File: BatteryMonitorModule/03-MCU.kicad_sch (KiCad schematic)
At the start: 0 parts

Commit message: schematic annotation and component placement for power supply, MCU, and power path sheets
Added symbol libraries (AP63203, AP63205, MIC5219, TC2117), annotated
ref designators, and placed components via MCP server. Includes
fix_sheet_instances.py utility for restoring sheet_instances blocks.

Co-Authored-By: Claude Opus 4.6 (1M context) <noreply@anthropic.com>
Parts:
- added C10, C6, C8, C9: 100nF, symbol Device:C
- added C7: 4.7uF, symbol Device:C
- added FB1: 600R@100MHz, symbol Device:L
- added J3: Conn_ARM_JTAG_SWD_10, symbol Connector:Conn_ARM_JTAG_SWD_10
- added J4: USB-C, symbol Connector:USB_C_Receptacle
- added R10: 10k, symbol Device:R
- added R11, R12, R13, R14: 4k7, symbol Device:R
- added R14, R15: 5k1, symbol Device:R
- added SW1: BOOT0, symbol Switch:SW_Push
- added SW2: NRST, symbol Switch:SW_Push
- added U1: STM32G0B1CCT6, symbol MCU_ST_STM32G0:STM32G0B1CCTx
- added U2: INA226AQDGSRQ1, symbol INA226AQDGSRQ1:INA226AQDGSRQ1
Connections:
- new net: FB1.1, U2.7 (GND)
- new net: J4.A5 (CC1), R14.1
- new net: J4.B5 (CC2), R15.1
- new net +3.3V: C10.1, C6.1, C7.1, C9.2, J3.1 (VTref), R11.1, R12.1, R13.1, R14.1, SW1.2, U1.4 (VBAT), U1.5 (VREF+), U1.6 (VDD), U2.6 (VS)
- new net +5VUsb: J4.A4 (VBUS), J4.A9 (VBUS), J4.B4 (VBUS), J4.B9 (VBUS)
- new net BOOT0/SWDCLK: J3.4 (SWCLK/TCK), R10.1, SW1.1, U1.36 (PA14)
- new net GND: C6.2, C7.2, C8.1, C9.1, FB1.2, J3.3 (GND), J3.5 (GND), J3.8 (NC/TDI), J3.9 (GNDDetect), J4.A1 (GND), J4.A10 (RX2-), J4.A11 (RX2+), J4.A12 (GND), J4.A2 (TX1+), J4.A3 (TX1-), J4.A8 (SBU1), J4.B1 (GND), J4.B10 (RX1-), J4.B11 (RX1+), J4.B12 (GND), J4.B2 (TX2+), J4.B3 (TX2-), J4.B8 (SBU2), J4.S1 (SHIELD), R10.2, R14.2, R15.2, SW2.1, U1.7 (VSS), U2.1 (A1), U2.2 (A0)
- new net I2C1_SCL: R11.2
- new net I2C1_SDA: R12.2
- new net I2C2_SCL: R13.2
- new net I2C2_SDA: R14.2
- new net INA_ALERT: U1.19 (PB0)
- new net N_RST: C8.2, J3.10 (~{RESET}), SW2.2, U1.10 (PF2)
- new net SHUNT_N: U2.9 (VIN-)
- new net SHUNT_P: U2.10 (VIN+), U2.8 (VBUS)
- new net SWDIO: J3.2 (SWDIO/TMS), U1.35 (PA13)
- new net SWO: J3.6 (SWO/TDO)
- new net USB_DN: J4.A7 (D-), J4.B7 (D-), U1.33 (PA9/PA11)
- new net USB_DP: J4.A6 (D+), J4.B6 (D+), U1.34 (PA10/PA12)
- new net VBUS_SENSE: U1.29 (PA9/UCPD1_DBCC1)
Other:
- note added: "I2C 0x40"
- note added: "I2C Pull Ups"

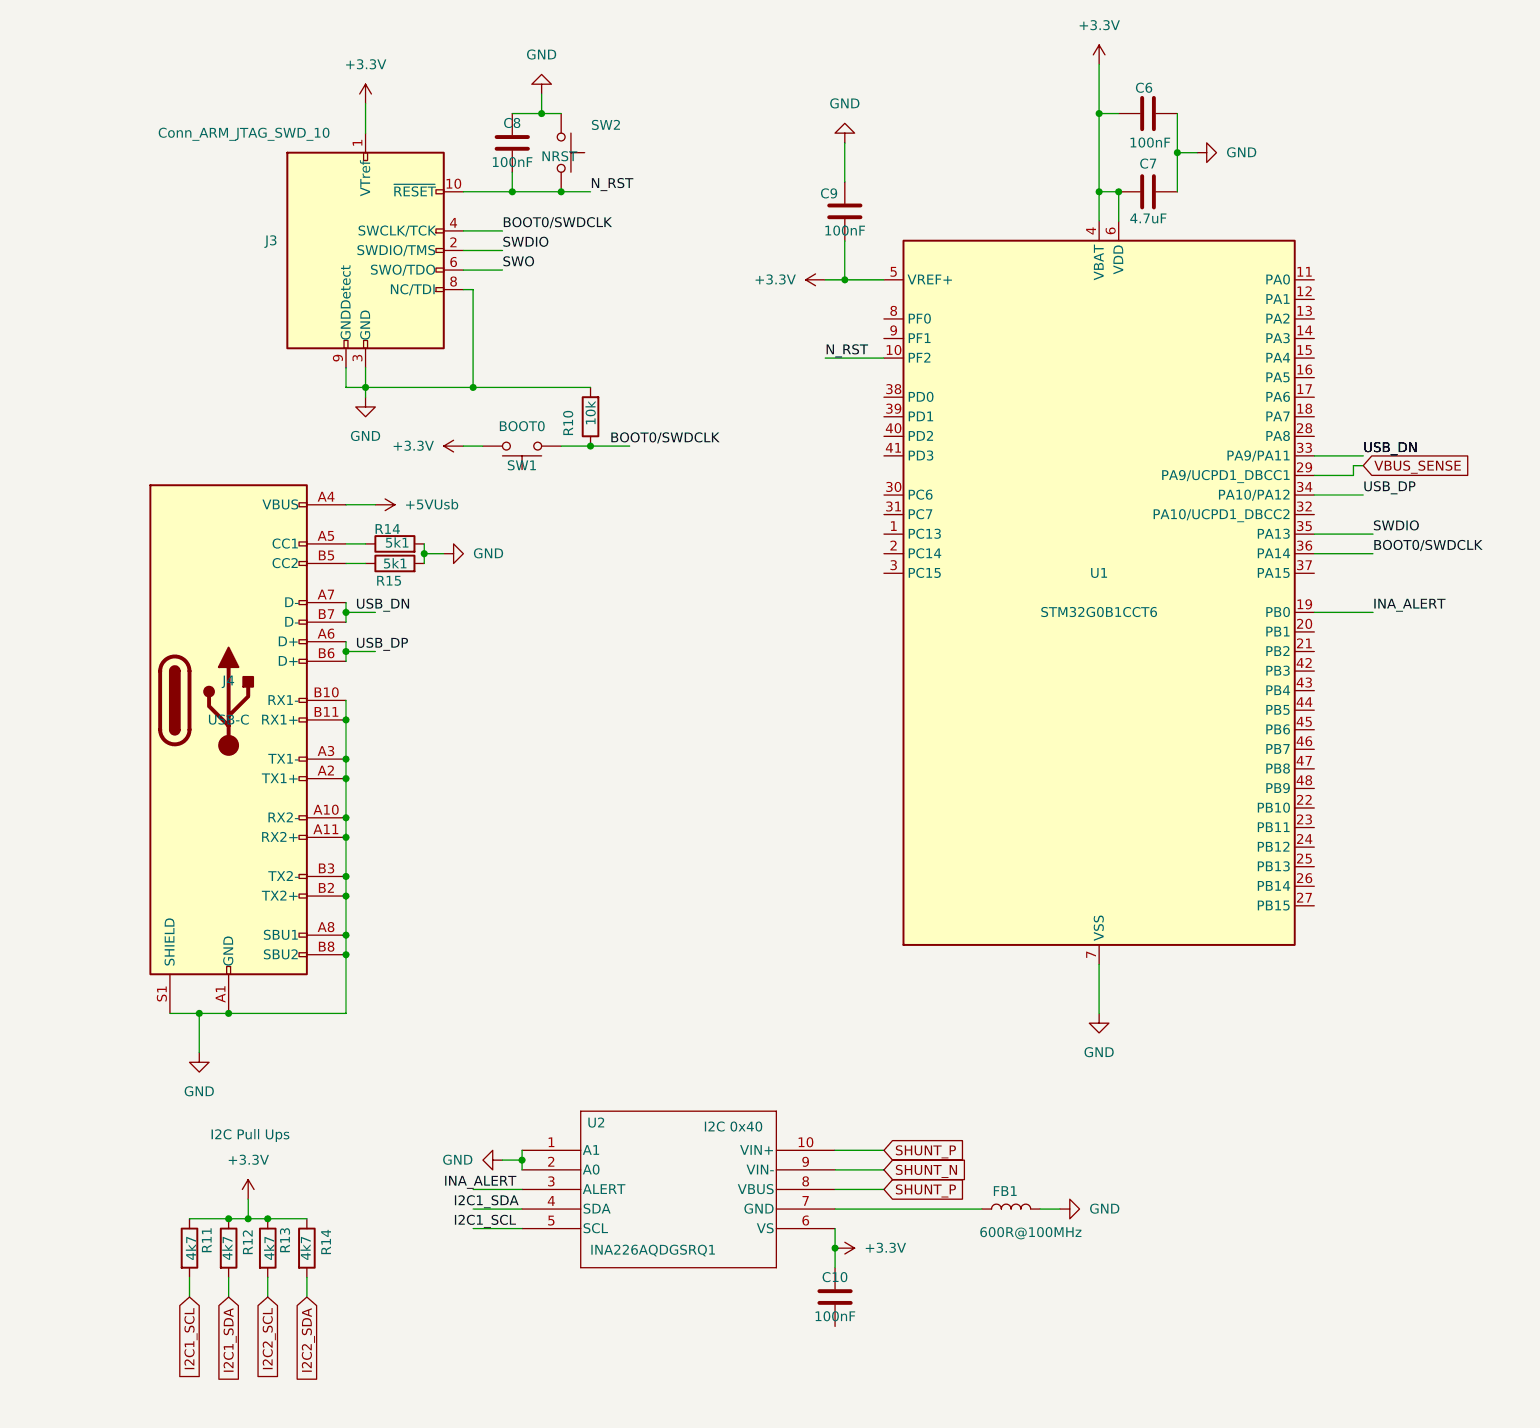
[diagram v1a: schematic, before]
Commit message: updated MCU schematic — additional component placement and wiring
Co-Authored-By: Claude Opus 4.6 (1M context) <noreply@anthropic.com>
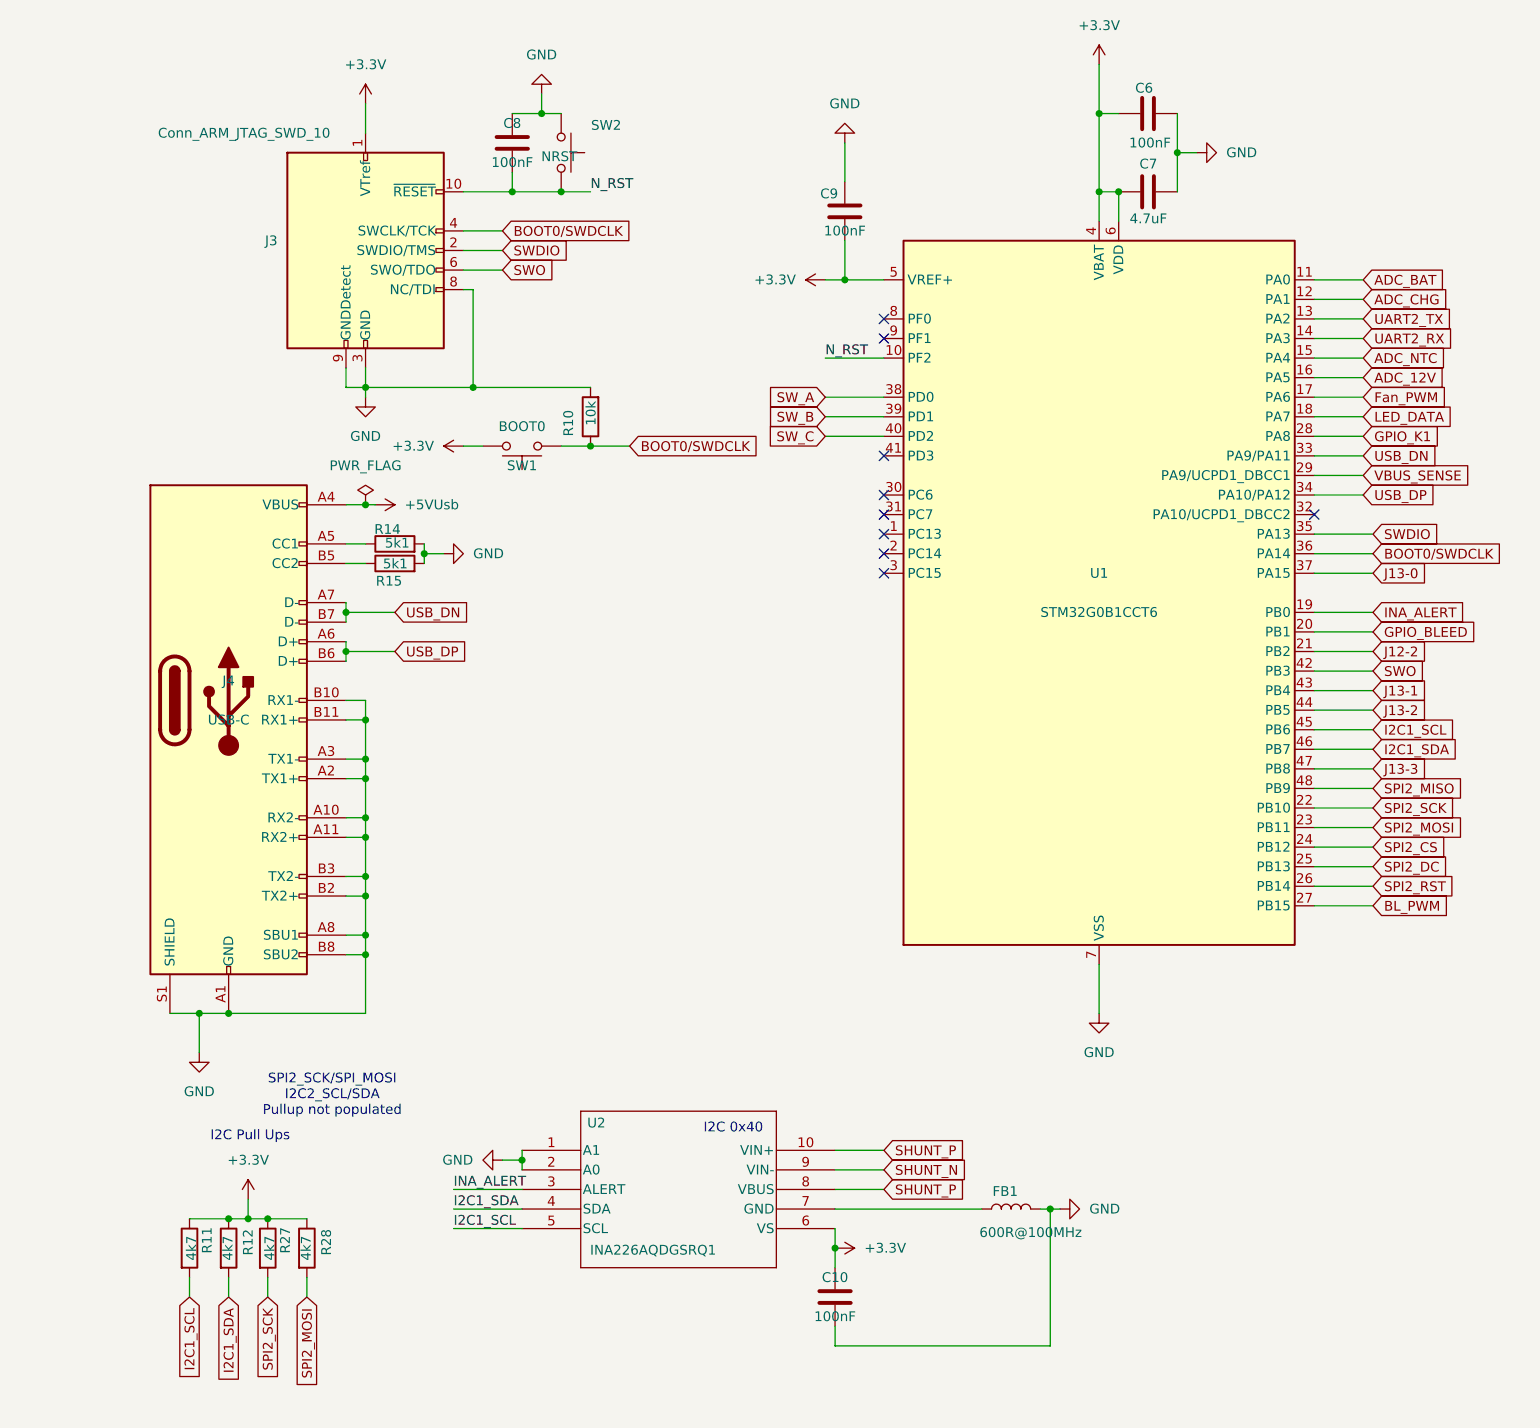
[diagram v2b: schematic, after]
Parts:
- renumbered R13 to R27, R14 to R28
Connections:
- net I2C2_SCL is gone; now on net SPI2_SCK: R27.2
- net GND: now also C10.2
- net I2C1_SCL: now also U1.45 (PB6), U2.5 (SCL)
- net I2C1_SDA: now also U1.46 (PB7), U2.4 (SDA)
- net INA_ALERT: now also U2.3 (ALERT)
- net SWO: now also U1.42 (PB3)
- net ADC_BAT: now reaches U1.11 (PA0)
- net ADC_CHG: now reaches U1.12 (PA1)
- net UART2_TX: now reaches U1.13 (PA2)
- net UART2_RX: now reaches U1.14 (PA3)
- net ADC_NTC: now reaches U1.15 (PA4)
- net ADC_12V: now reaches U1.16 (PA5)
- net Fan_PWM: now reaches U1.17 (PA6)
- net LED_DATA: now reaches U1.18 (PA7)
- net GPIO_BLEED: now reaches U1.20 (PB1)
- net J12-2: now reaches U1.21 (PB2)
- net SPI2_SCK: now reaches U1.22 (PB10)
- net SPI2_MOSI: now reaches U1.23 (PB11)
- net SPI2_CS: now reaches U1.24 (PB12)
- net SPI2_DC: now reaches U1.25 (PB13)
- net SPI2_RST: now reaches U1.26 (PB14)
- net BL_PWM: now reaches U1.27 (PB15)
- net GPIO_K1: now reaches U1.28 (PA8)
- net J13-0: now reaches U1.37 (PA15)
- net SW_A: now reaches U1.38 (PD0)
- net SW_B: now reaches U1.39 (PD1)
- net SW_C: now reaches U1.40 (PD2)
- net J13-1: now reaches U1.43 (PB4)
- net J13-2: now reaches U1.44 (PB5)
- net J13-3: now reaches U1.47 (PB8)
- net SPI2_MISO: now reaches U1.48 (PB9)
- net I2C2_SDA renamed SPI2_MOSI 
- no-connect marks 0 -> 9
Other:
- note added: "SPI2_SCK/SPI_MOSI I2C2_SCL/SDA Pullup not populated"

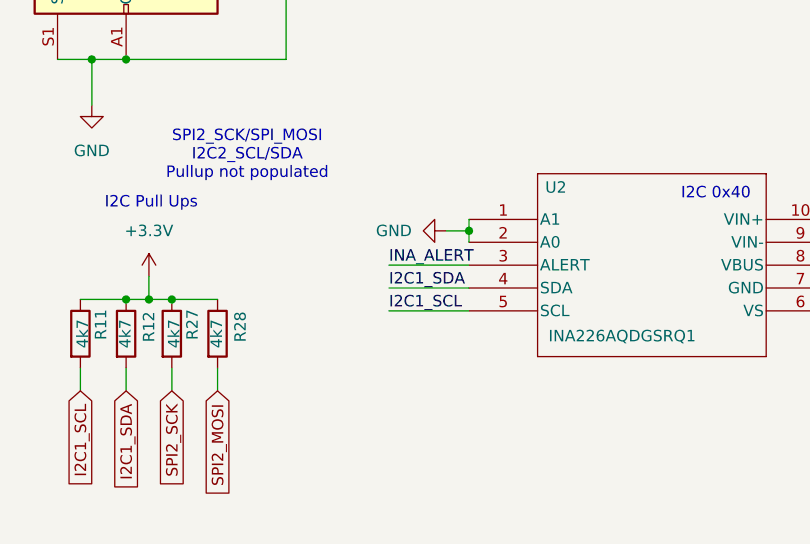
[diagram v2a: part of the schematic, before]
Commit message: updated schematics — MCU and IO wiring updates, sheet instance fixes
Co-Authored-By: Claude Opus 4.6 (1M context) <noreply@anthropic.com>
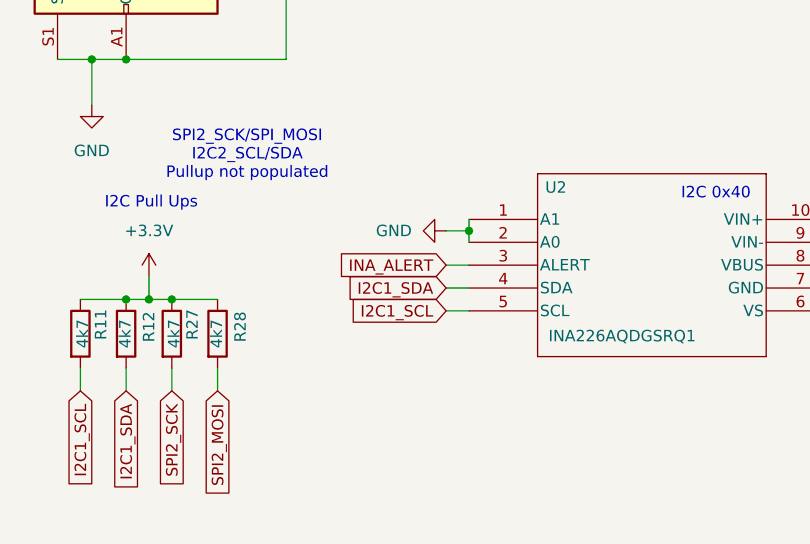
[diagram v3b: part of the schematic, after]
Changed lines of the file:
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@@
 	(wire
 		(pts
-			(xy 57.15 171.45) (xy 66.04 171.45)
+			(xy 63.5 171.45) (xy 66.04 171.45)
 		)
 		(stroke
@@
 	(wire
 		(pts
-			(xy 57.15 168.91) (xy 66.04 168.91)
+			(xy 63.5 168.91) (xy 66.04 168.91)
 		)
 		(stroke
@@
 	(wire
 		(pts
-			(xy 57.15 173.99) (xy 66.04 173.99)
+			(xy 63.5 173.99) (xy 66.04 173.99)
 		)
 		(stroke
@@
 		)
 	)
-	(label "I2C1_SDA"
-		(at 57.15 171.45 0)
-		(effects
-			(font
-				(size 1.27 1.27)
-			)
-			(justify left bottom)
-		)
-	)
-	(label "INA_ALERT"
-		(at 57.15 168.91 0)
-		(effects
-			(font
-				(size 1.27 1.27)
-			)
-			(justify left bottom)
-		)
-	)
-	(label "I2C1_SCL"
-		(at 57.15 173.99 0)
-		(effects
-			(font
-				(size 1.27 1.27)
-			)
-			(justify left bottom)
-		)
-	)
 	(label "N_RST"
 		(at 74.93 39.37 0)
@@
 		)
 	)
+	(global_label "INA_ALERT"
+		(shape input)
+		(at 63.5 168.91 180)
+		(fields_autoplaced yes)
+		(effects
+			(font
+				(size 1.27 1.27)
+			)
+			(justify right)
+		)
+		(property "Intersheetrefs" "${INTERSHEET_REFS}"
+			(at 51.02 168.91 0)
+			(effects
+				(font
+					(size 1.27 1.27)
+				)
+				(justify right)
+				(hide yes)
+			)
+		)
+	)
 	(global_label "ADC_NTC"
 		(shape input)
@@
 		)
 	)
+	(global_label "I2C1_SCL"
+		(shape input)
+		(at 63.5 173.99 180)
+		(fields_autoplaced yes)
+		(effects
+			(font
+				(size 1.27 1.27)
+			)
+			(justify right)
+		)
+		(property "Intersheetrefs" "${INTERSHEET_REFS}"
+			(at 51.7458 173.99 0)
+			(effects
+				(font
+					(size 1.27 1.27)
+				)
+				(justify right)
+				(hide yes)
+			)
+		)
+	)
 	(global_label "SW_C"
 		(shape input)
@@
 		)
 	)
+	(global_label "I2C1_SDA"
+		(shape input)
+		(at 63.5 171.45 180)
+		(fields_autoplaced yes)
+		(effects
+			(font
+				(size 1.27 1.27)
+			)
+			(justify right)
+		)
+		(property "Intersheetrefs" "${INTERSHEET_REFS}"
+			(at 51.6853 171.45 0)
+			(effects
+				(font
+					(size 1.27 1.27)
+				)
+				(justify right)
+				(hide yes)
+			)
+		)
+	)
 	(global_label "ADC_BAT"
 		(shape input)
@@
 		)
 	)
+	(sheet_instances
+		(path "/c3000003-0000-0000-0000-000000000003"
+			(page "4")
+		)
+	)

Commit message: updated all schematics — IO sheet wiring, MCU connections, power supply refinements, custom footprints
Co-Authored-By: Claude Opus 4.6 (1M context) <noreply@anthropic.com>
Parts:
- C10, C6, C8, C9: footprint (none) -> Capacitor_SMD:C_0603_1608Metric
- C7: footprint (none) -> Capacitor_SMD:C_0805_2012Metric
- FB1: footprint (none) -> Inductor_SMD:L_0603_1608Metric
- J3: footprint (none) -> Connector_PinHeader_1.27mm:PinHeader_2x05_P1.27mm_Vertical_SMD
- J4: footprint (none) -> Connector_USB:USB_C_Receptacle_GCT_USB4085
- R10, R11, R12, R14, R15, R27, R28: footprint (none) -> Resistor_SMD:R_0603_1608Metric
- SW1, SW2: footprint (none) -> BatteryMonitorModule_Custom:SWITCH_FSMSM_TYC
- U1: footprint (none) -> Package_QFP:LQFP-48_7x7mm_P0.5mm
- U2: footprint (none) -> Package_SO:MSOP-10_3x3mm_P0.5mm
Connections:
- net SPI2_MOSI  is gone; now on net SPI2_MOSI: R28.2
- net GND: now also J4.SH (SHIELD); no longer J3.8 (NC/TDI), J4.S1 (SHIELD)
- net J13-5: now reaches U1.1 (PC13)
- net J12-0: now reaches U1.30 (PC6)
- net J12-1: now reaches U1.31 (PC7)
- net MCU_HB: now reaches U1.32 (PA10/UCPD1_DBCC2)
- net J13-4: now reaches U1.41 (PD3)
- net Fan_PWM renamed FAN_PWM
- no-connect marks 9 -> 5

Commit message: added connector footprints and power path updates
New custom footprints: OSTYK screw terminals, KF8500 connectors, USB4085-GF-A.
Power path schematic updates and project library references.

Co-Authored-By: Claude Opus 4.6 (1M context) <noreply@anthropic.com>
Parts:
- J4: footprint Connector_USB:USB_C_Receptacle_GCT_USB4085 -> BatteryMonitorModule_Custom:USB4085-GF-A_GCT
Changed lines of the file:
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@@
 			)
 		)
-		(property "Footprint" "Connector_USB:USB_C_Receptacle_GCT_USB4085"
+		(property "Footprint" "BatteryMonitorModule_Custom:USB4085-GF-A_GCT"
 			(at 27.94 105.41 0)
 			(hide yes)
